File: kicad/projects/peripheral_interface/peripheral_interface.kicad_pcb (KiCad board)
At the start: 2 copper layers, 203.2 x 97.8 mm, 42 parts, among them J1 Pi Pico Standin, J2 VOLTAGE CONVERTER, J3 OLED SCREEN, J4 BACKPLANE AUX, J5 BACKPLANE BANK, J6 BACKPLANE BUS, J7 TO CPU, J8 FROM CPU, J9 KEYPAD, U1 74HC595, U10 74HC597, U11 74HC157, U12 74HC157, U13 74HCT245, U14 74HC597, U2 74HC595, U3 74HC595, U4 74HC595, U5 74HC595, U6 74HC595, U7 74HC597, U8 74HC597, U9 74HC597

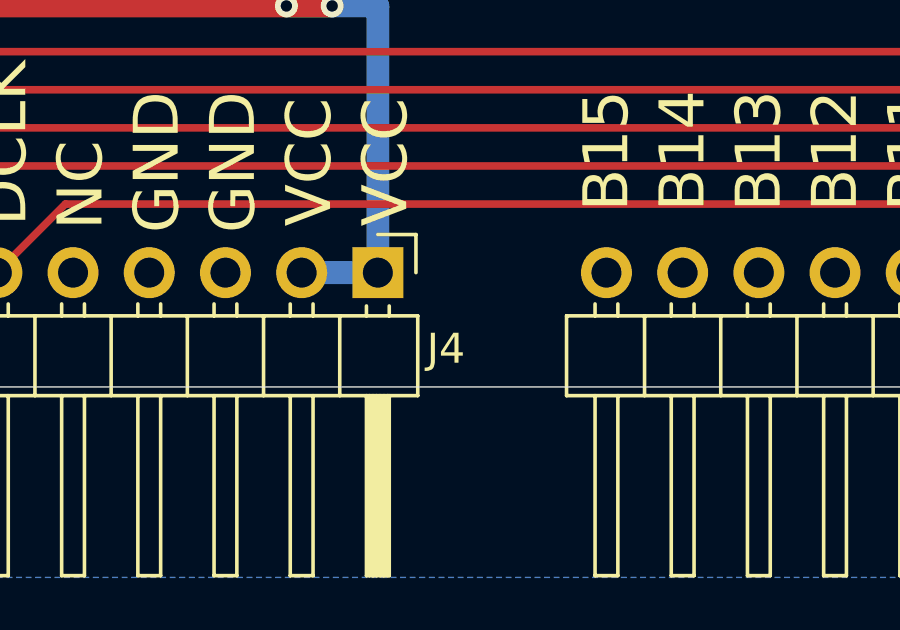
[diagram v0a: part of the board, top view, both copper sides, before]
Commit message: Peripheral connect updated to one wire rfm wtm.
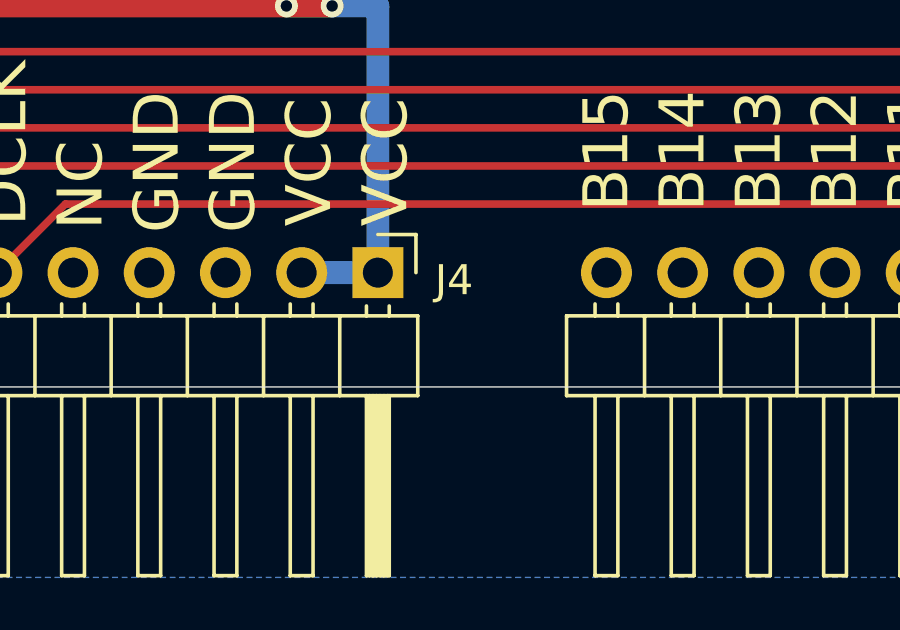
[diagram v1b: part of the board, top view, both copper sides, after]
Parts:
- J4: value BACKPLANE AUX -> peripheral_aux_connector

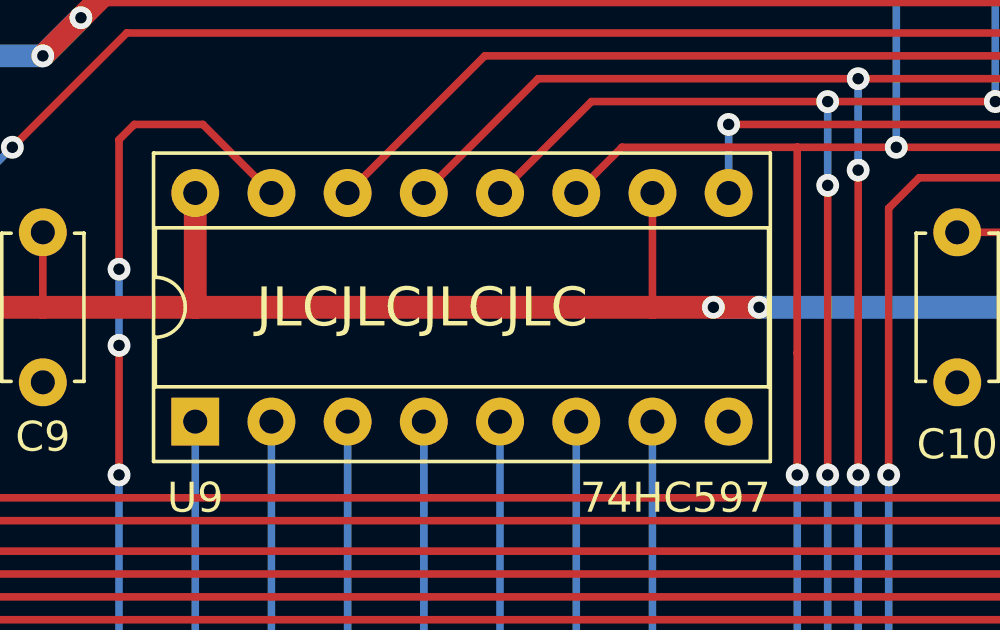
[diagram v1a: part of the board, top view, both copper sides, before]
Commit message: Interface clock bus connector updated.
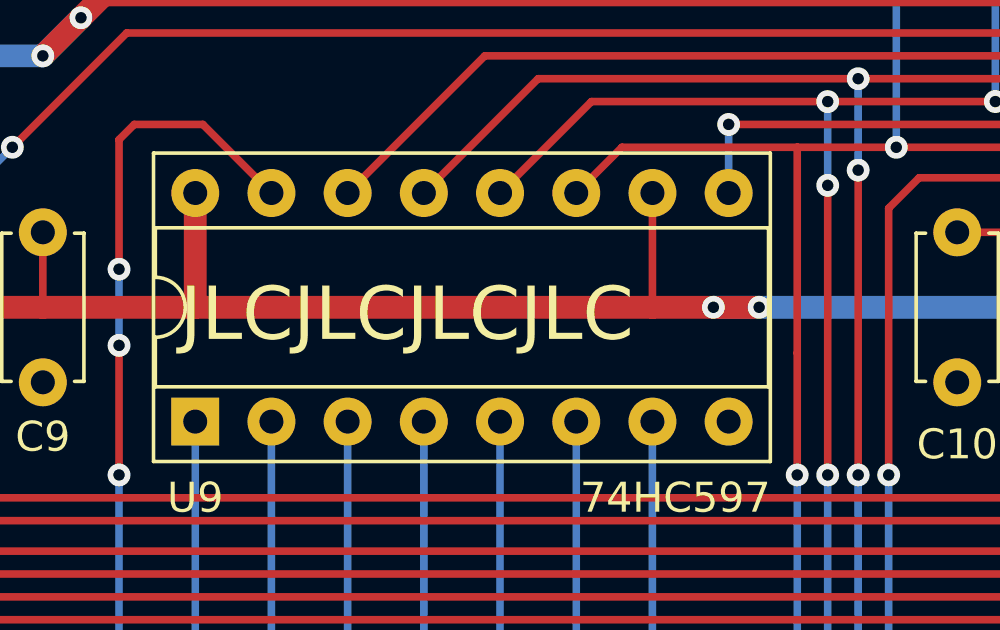
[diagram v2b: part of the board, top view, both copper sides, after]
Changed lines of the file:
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@@
     (effects (font (size 1.27 1.27) (thickness 0.2032)) (justify left bottom))
   )
-  (gr_text "JLCJLCJLCJLC" (at 123.952 83.312) (layer "F.SilkS")
-    (effects (font (size 1.3 1.3) (thickness 0.2)) (justify left bottom))
+  (gr_text "JLCJLCJLCJLC" (at 121.412 83.82) (layer "F.SilkS")
+    (effects (font (size 1.778 1.778) (thickness 0.254)) (justify left bottom))
   )
   (gr_text "7" (at 90.932 76.454) (layer "F.SilkS")

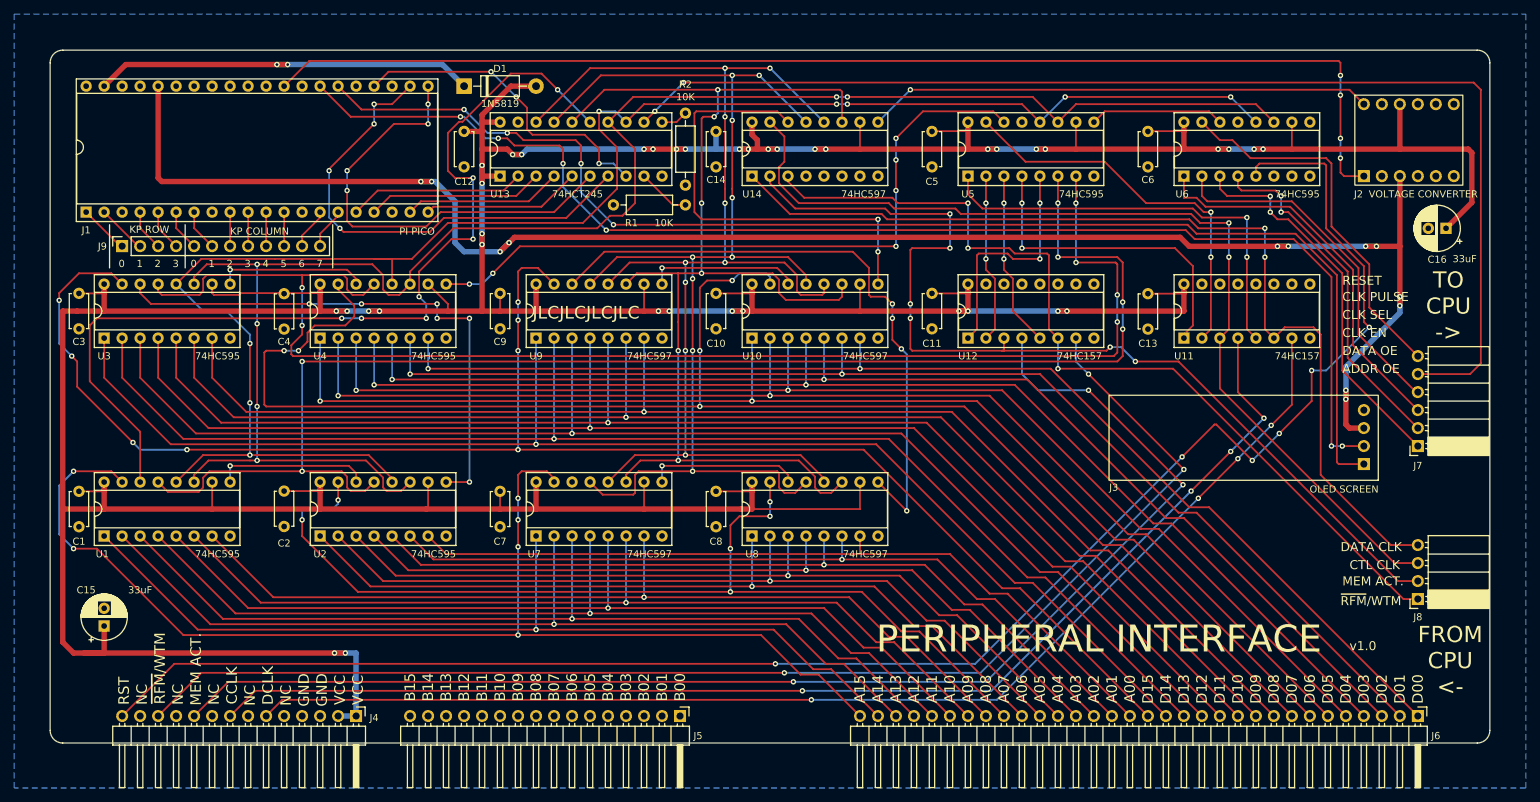
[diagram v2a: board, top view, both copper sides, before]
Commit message: Update peripheral interface.
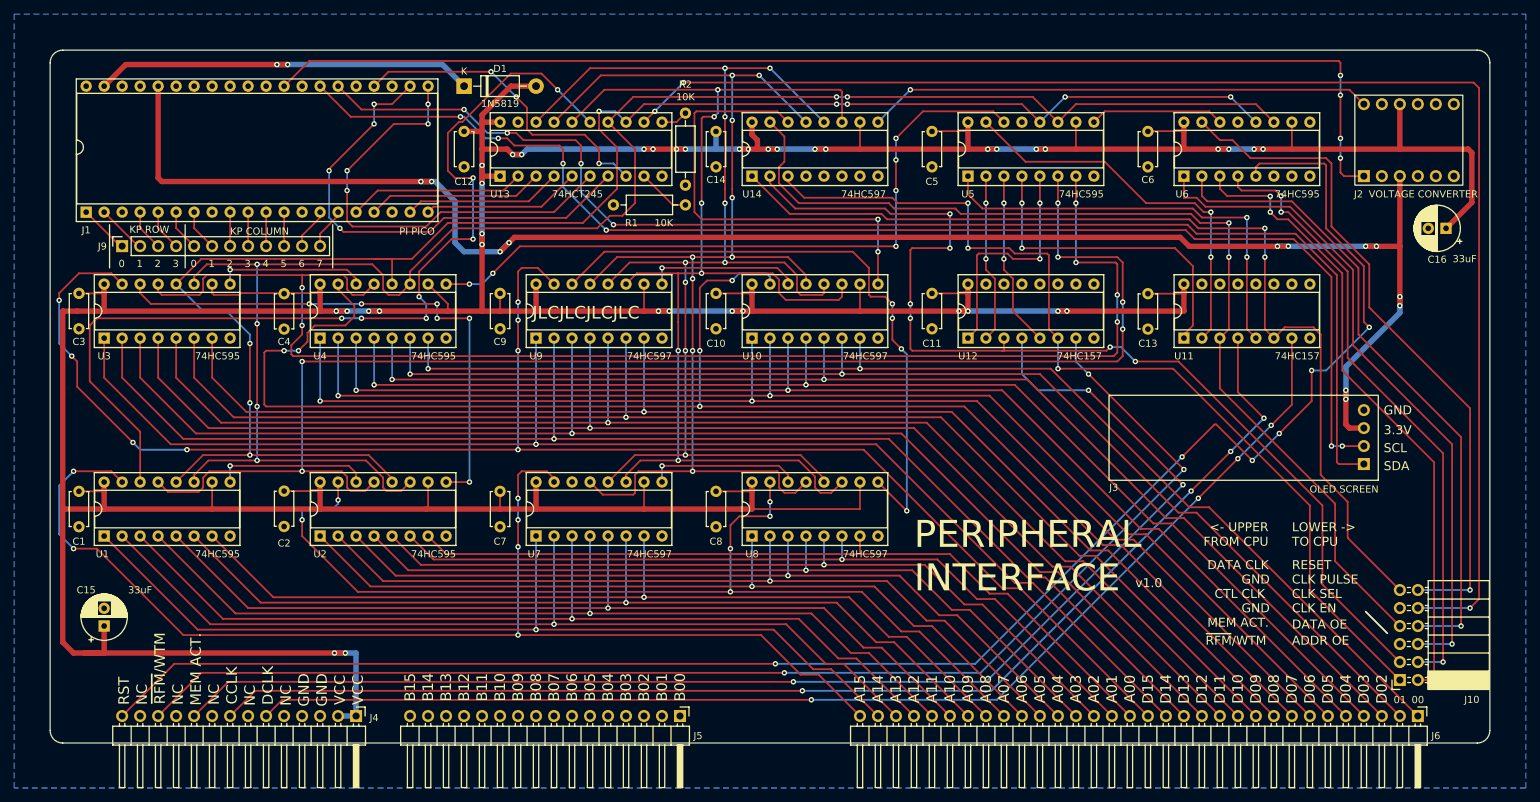
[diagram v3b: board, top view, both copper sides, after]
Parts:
- removed J7: TO CPU, Connector_PinSocket_2.54mm:PinSocket_1x06_P2.54mm_Horizontal
- removed J8: FROM CPU, Connector_PinSocket_2.54mm:PinSocket_1x04_P2.54mm_Horizontal
- added J10: CPU CONNECT, Connector_PinSocket_2.54mm:PinSocket_2x06_P2.54mm_Horizontal, F.Cu at (243.8, 134.6)
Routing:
- net /RESET_TO_CPU: track 52.9 -> 96.4 mm, vias 0 -> 1
- net /CLK_SEL_TO_CPU: track 50.2 -> 91.7 mm, vias 0 -> 1
- net /CLK_EN_TO_CPU: track 54.7 -> 94.6 mm, vias 0 -> 1
- net /DATA_OE_TO_CPU: track 49.5 -> 87.6 mm, vias 2 -> 3
- net /ADDR_OE_TO_CPU: track 54.1 -> 90.4 mm
- net /CLK_PULSE_5V: track 169.0 -> 201.8 mm, vias 2 -> 3
- net /RFM_WTM_FROM_CPU: track 126.4 -> 135.6 mm
- net /MEM_ACT_FROM_CPU: track 140.3 -> 149.1 mm
- net /CTL_CLK_FROM_CPU: track 137.6 -> 143.6 mm
- net /DATA_CLK_FROM_CPU: track 136.7 -> 139.8 mm
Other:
- board text added: "3.3V"
- board text added: "<- UPPER FROM CPU"
- board text added: "GND"
- board text added: "LOWER -> TO CPU"
- board text added: "SCL"
- board text added: "SDA"
- board text removed: "FROM CPU <-"
- board text removed: "TO CPU ->"

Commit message: Tech checks complete on peripheral interface.
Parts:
- added R3: 10K, Resistor_THT:R_Axial_DIN0207_L6.3mm_D2.5mm_P2.54mm_Vertical, F.Cu at (203.7, 75.4)
- added R4: 10K, Resistor_THT:R_Axial_DIN0207_L6.3mm_D2.5mm_P2.54mm_Vertical, F.Cu at (209.8, 75.4)
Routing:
- net /INTERFACE_DATA_ASSERT: track 195.9 -> 205.7 mm, vias 6 -> 7
- net VCC: track 766.3 -> 773.3 mm
- net /MEM_ACT: track 187.4 -> 191.2 mm
- net /~{RFM}/WTM: track 184.0 -> 186.2 mm
- net /RFM_WTM_FROM_CPU: track 135.6 -> 133.5 mm
- net /SERIAL_READ_DATA_3V3: track 169.7 -> 168.6 mm
- net /DATA_BUS_15: track 226.7 -> 226.0 mm
- net /SERIAL_READ_SHIFT_CLK_5V: track 170.1 -> 170.7 mm
- net /INTERFACE_ADDR_ASSERT: track 201.4 -> 202.0 mm

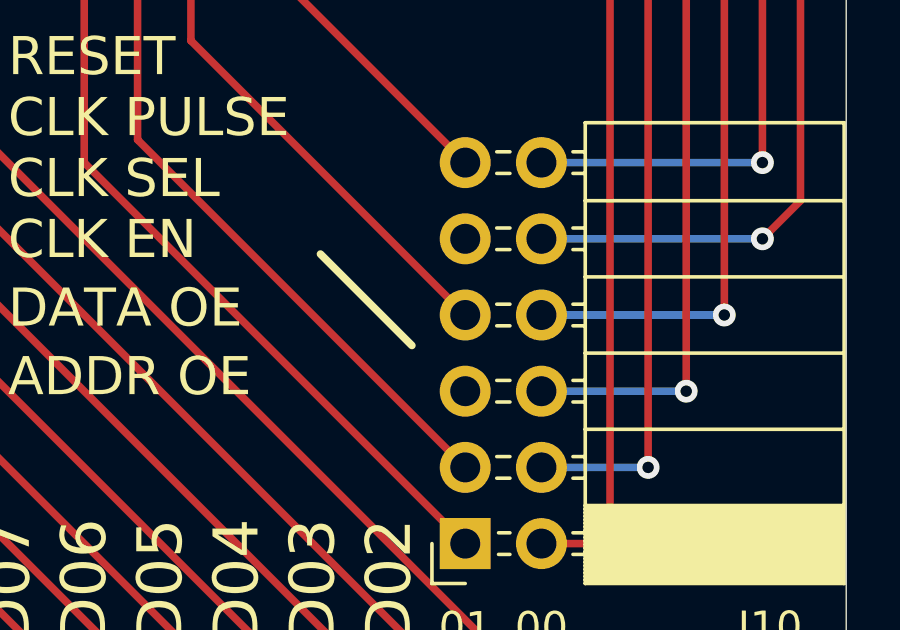
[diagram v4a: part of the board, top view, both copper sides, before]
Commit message: Generate peripheral gerbers.
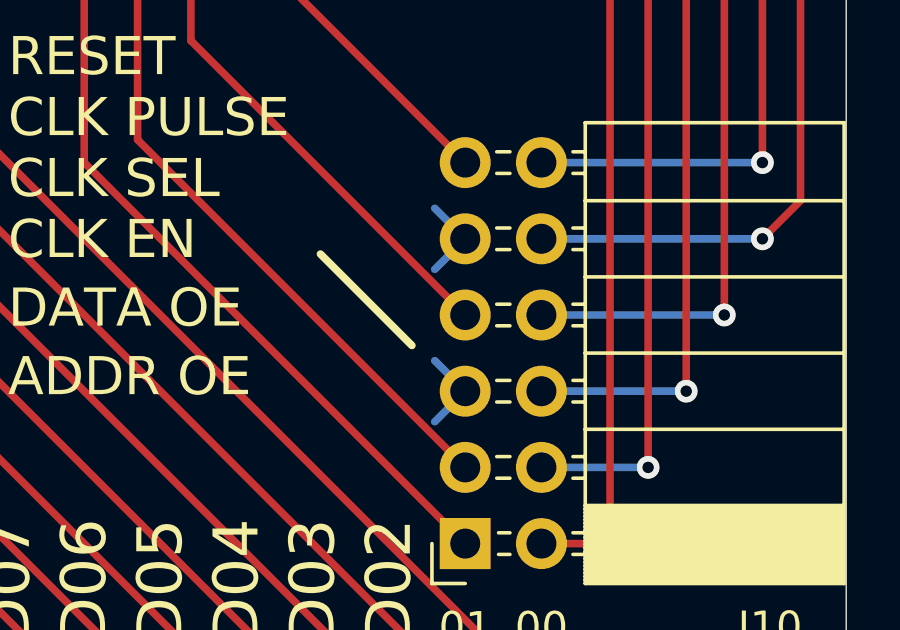
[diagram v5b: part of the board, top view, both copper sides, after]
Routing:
- net GND: track 0.00 -> 5.75 mm
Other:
- rule pad_to_mask_clearance: 0.051 -> 0
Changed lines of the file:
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@@
       (dielectric_constraints no)
     )
-    (pad_to_mask_clearance 0.051)
-    (solder_mask_min_width 0.25)
+    (pad_to_mask_clearance 0)
     (pcbplotparams
       (layerselection 0x00010fc_ffffffff)
       (plot_on_all_layers_selection 0x0000000_00000000)
       (disableapertmacros false)
-      (usegerberextensions false)
+      (usegerberextensions true)
       (usegerberattributes false)
       (usegerberadvancedattributes false)
@@
       (plotinvisibletext false)
       (sketchpadsonfab false)
-      (subtractmaskfromsilk false)
+      (subtractmaskfromsilk true)
       (outputformat 1)
       (mirror false)
-      (drillshape 1)
+      (drillshape 0)
       (scaleselection 1)
-      (outputdirectory "")
+      (outputdirectory "gerber_v1/")
     )
   )
@@
   (segment (start 158.496 132.334) (end 183.896 132.334) (width 0.254) (layer "B.Cu") (net 65))
   (segment (start 231.394 90.932) (end 233.426 90.932) (width 0.254) (layer "B.Cu") (net 65))
+  (segment (start 243.84 129.54) (end 242.824 130.556) (width 0.254) (layer "B.Cu") (net 72))
+  (segment (start 243.84 124.46) (end 242.824 123.444) (width 0.254) (layer "B.Cu") (net 72))
+  (segment (start 243.84 129.54) (end 242.824 128.524) (width 0.254) (layer "B.Cu") (net 72))
+  (segment (start 243.84 124.46) (end 242.824 125.476) (width 0.254) (layer "B.Cu") (net 72))
   (segment (start 153.162 59.69) (end 154.686 59.69) (width 0.762) (layer "F.Cu") (net 77))
   (segment (start 114.3 63.5) (end 116.84 63.5) (width 0.762) (layer "F.Cu") (net 77))
